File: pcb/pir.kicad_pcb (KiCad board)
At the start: 2 copper layers, 80 x 100 mm, 146 parts, among them IC1 MAX44009EDT+T, IC2 IRA-S210ST01, IC3 EL817S, IC4 EL817S, IC7 EL817S, IC8 EL817S, J1 SJ-2523-SMT-TR, J2 FH12-24S-0.5SH(55), J3 SWD, J4 UART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

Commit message: Routed what seem to be the last useful tracks
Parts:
- moved TP25 94.8 mm to (-145.8, 115.4)
- moved TP34 94.8 mm to (-141.7, 115.4)
- moved TP24 94.8 mm to (-137.2, 109.7)
- moved TP26 94.8 mm to (-133.1, 103.6)
- moved TP27 94.8 mm to (-146.9, 121.5)
- moved TP29 94.8 mm to (-151.0, 121.5)
- moved TP31 94.8 mm to (-155.1, 120.1)
- moved TP32 94.8 mm to (-137.2, 103.6)
- moved TP33 94.8 mm to (-159.1, 120.1)
- moved TP36 94.8 mm to (-129.0, 103.6)
- moved TP39 94.8 mm to (-133.6, 115.7)
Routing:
- net VCC: track 332.6 -> 444.3 mm, vias 4 -> 6
- net Net-(JP3-Pad2): track 15.6 -> 37.9 mm, vias 0 -> 1
- net Earth: track 18.7 -> 35.3 mm, vias 5 -> 6
- net /soc/EINK_MOSI: track 46.1 -> 49.3 mm
- net /sensor/OPAMP2+: track 38.6 -> 41.5 mm

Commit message: OK button MOVED TO A WKUP pin. PCB routing done.
DRC passed.
Unconnected tracks : 0.
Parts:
- removed TP24, TP25, TP26, TP27, TP31, TP32, TP33, TP34, TP36, TP39: TEST, Measurement_Points:Measurement_Point_Round-TH_Small
- TP11, TP12, TP13, TP15, TP16, TP17, TP18: footprint Measurement_Points:Measurement_Point_Round-TH_Small -> Measurement_Points:Measurement_Point_Round-SMD-Pad_Small
- moved TP29 267.1 mm to (108.4, 58.0)
- moved TP18 235.0 mm to (51.8, 66.4)
- moved TP17 232.3 mm to (53.6, 75.2)
- moved TP15 220.3 mm to (52.6, 71.6)
- moved TP12 218.2 mm to (50.2, 69.0)
- moved TP11 214.8 mm to (50.4, 74.6)
- moved TP13 206.0 mm to (48.0, 71.6)
- moved TP16 200.6 mm to (48.6, 65.6)
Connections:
- U1 pad 25: Net-(TP24-Pad1) -> /soc/OK
- U1 pad 39: /soc/OK -> Net-(U1-Pad39)
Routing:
- net /soc/OK: track 25.5 -> 33.0 mm
- net Earth: track 35.3 -> 41.7 mm, vias 6 -> 9
- net Net-(C41-Pad1): track 7.33 -> 11.7 mm
- net Net-(C8-Pad1): track 0.00 -> 3.62 mm
- net Net-(C38-Pad2): track 77.9 -> 81.1 mm
- net /soc/EINK_BS: track 46.0 -> 46.8 mm, vias 2 -> 3
- net /soc/EINK_D/C: track 39.9 -> 40.1 mm, vias 2 -> 3
- net VCC: track 444.3 -> 444.1 mm, vias 6 -> 7
- net /soc/EINK_SCK: vias 4 -> 5
- net /soc/EINK_MOSI: vias 2 -> 3
- net /soc/EINK_CS: vias 2 -> 3
- net /soc/EINK_BUSY: vias 2 -> 3
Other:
- rule trace_min: 0.1 -> 0.25

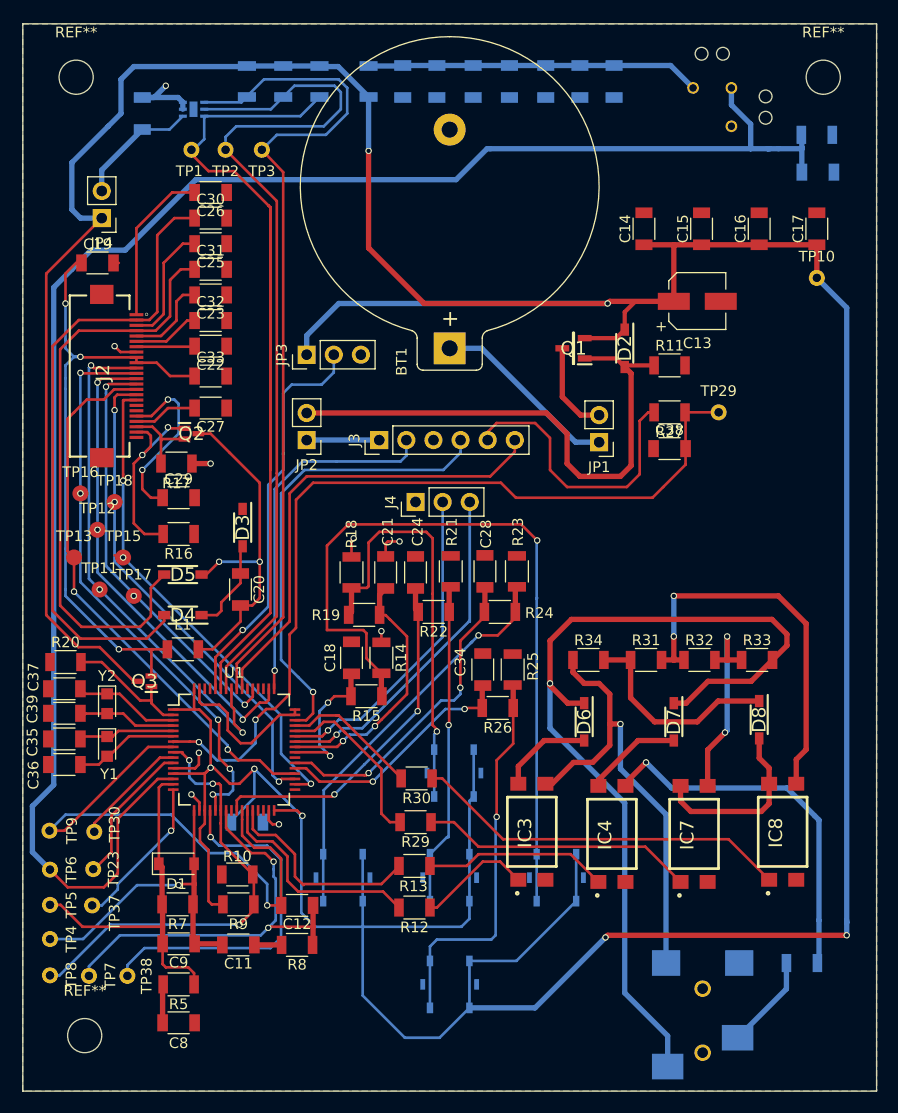
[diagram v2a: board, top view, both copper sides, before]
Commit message: 1 mounting hole was missing for some reason
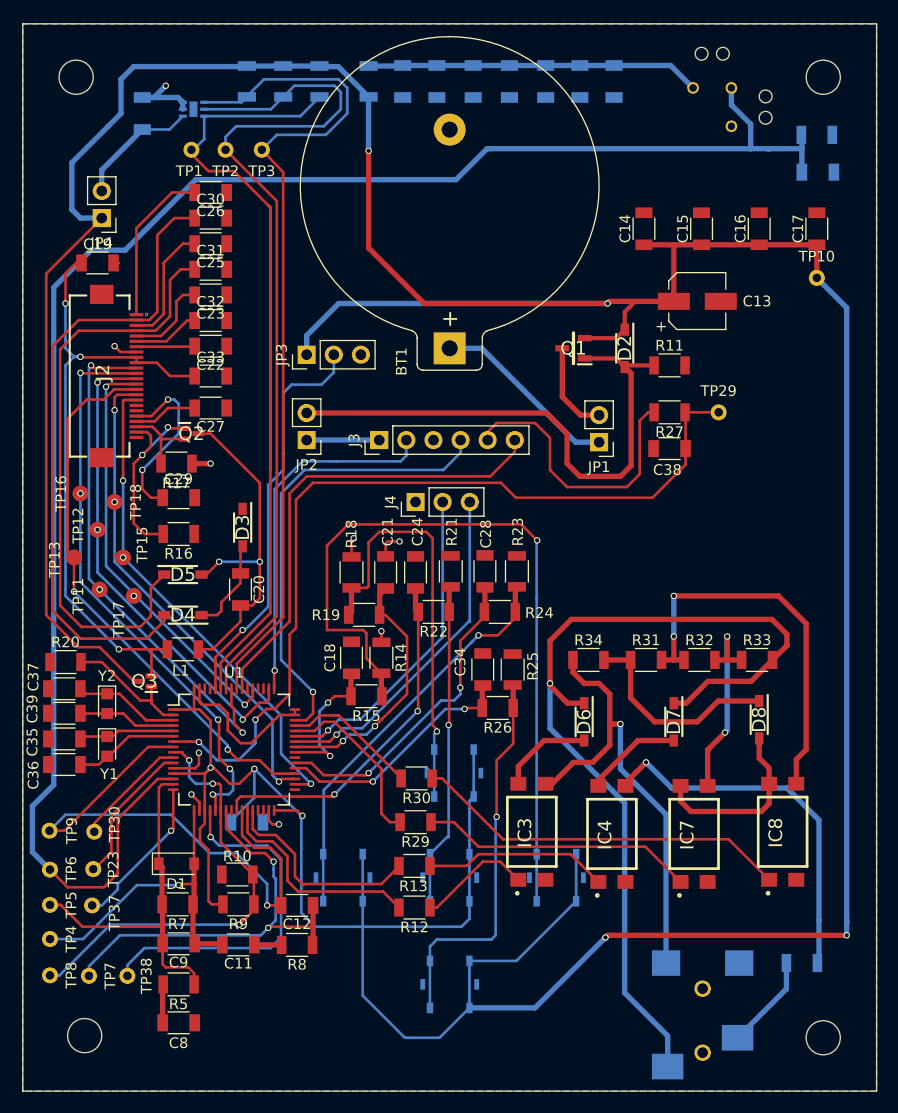
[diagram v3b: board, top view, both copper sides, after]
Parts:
- added REF**: MountingHole_3.2mm_M3, Mounting_Holes:MountingHole_3.2mm_M3, F.Cu at (118.2, 116.6)
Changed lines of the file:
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@@
     (tracks 1050)
     (zones 0)
-    (modules 136)
+    (modules 137)
     (nets 100)
   )
@@
     (add_net nRESET)
   )
+  (module Mounting_Holes:MountingHole_3.2mm_M3 locked (layer F.Cu)
+    (at 118.2 116.6)
+    (descr "Mounting Hole 3.2mm, no annular, M3")
+    (tags "mounting hole 3.2mm no annular m3")
+    (attr virtual)
+    (fp_text reference REF** (at 0 -4.2) (layer F.SilkS) hide
+      (effects (font (size 1 1) (thickness 0.15)))
+    )
+    (fp_text value MountingHole_3.2mm_M3 (at 0 4.2) (layer F.Fab)
+      (effects (font (size 1 1) (thickness 0.15)))
+    )
+    (fp_text user %R (at 0.3 0) (layer F.Fab)
+      (effects (font (size 1 1) (thickness 0.15)))
+    )
+    (fp_circle (center 0 0) (end 3.2 0) (layer Cmts.User) (width 0.15))
+    (fp_circle (center 0 0) (end 3.45 0) (layer F.CrtYd) (width 0.05))
+    (pad 1 np_thru_hole circle (at 0 0) (size 3.2 3.2) (drill 3.2) (layers *.Cu *.Mask))
+  )
   (module Capacitors_SMD:C_1206 (layer B.Cu)
     (at 64.2 96.4 180)
@@
     (tags "mounting hole 3.2mm no annular m3")
     (attr virtual)
-    (fp_text reference REF** (at 0 -4.2) (layer F.SilkS)
+    (fp_text reference REF** (at 0 -4.2) (layer F.SilkS) hide
       (effects (font (size 1 1) (thickness 0.15)))
     )
@@
     (tags "mounting hole 3.2mm no annular m3")
     (attr virtual)
-    (fp_text reference REF** (at 0 -4.2) (layer F.SilkS)
+    (fp_text reference REF** (at 0 -4.2) (layer F.SilkS) hide
       (effects (font (size 1 1) (thickness 0.15)))
     )
@@
     (descr "SMT capacitor, aluminium electrolytic, 5x5.3")
     (attr smd)
-    (fp_text reference C13 (at 0 3.92) (layer F.SilkS)
+    (fp_text reference C13 (at 5.6 0) (layer F.SilkS)
       (effects (font (size 1 1) (thickness 0.15)))
     )
@@
       (effects (font (size 1 1) (thickness 0.15)))
     )
-    (fp_text user %R (at 0 3.92) (layer F.Fab)
+    (fp_text user %R (at 0 0.2 90) (layer F.Fab)
       (effects (font (size 1 1) (thickness 0.15)))
     )
@@
     (tags "capacitor 1206")
     (attr smd)
-    (fp_text reference C38 (at 0 -1.75) (layer F.SilkS)
+    (fp_text reference C38 (at -0.2 2) (layer F.SilkS)
       (effects (font (size 1 1) (thickness 0.15)))
     )
@@
       (effects (font (size 1 1) (thickness 0.15)))
     )
-    (fp_text user %R (at 0 -1.75) (layer F.Fab)
+    (fp_text user %R (at 0 0) (layer F.Fab)
       (effects (font (size 1 1) (thickness 0.15)))
     )
@@
     (fp_line (start 1.8 4.35) (end 1.8 -1.8) (layer F.CrtYd) (width 0.05))
     (fp_line (start 1.8 -1.8) (end -1.8 -1.8) (layer F.CrtYd) (width 0.05))
-    (fp_text user %R (at 0 1.27 270) (layer F.Fab)
+    (fp_text user %R (at 0 1.2 270) (layer F.Fab)
       (effects (font (size 1 1) (thickness 0.15)))
     )
@@
     (tags "mounting hole 3.2mm no annular m3")
     (attr virtual)
-    (fp_text reference REF** (at 0 -4.2) (layer F.SilkS)
+    (fp_text reference REF** (at 0 -4.2) (layer F.SilkS) hide
       (effects (font (size 1 1) (thickness 0.15)))
     )
@@
     (tags "resistor 1206")
     (attr smd)
-    (fp_text reference L1 (at 0 -2.3) (layer F.SilkS)
+    (fp_text reference L1 (at -0.2 2) (layer F.SilkS)
       (effects (font (size 1 1) (thickness 0.15)))
     )
@@
     (tags "Mesurement Point Round SMD Pad 1.5mm")
     (attr virtual)
-    (fp_text reference TP11 (at 0 -2) (layer F.SilkS)
+    (fp_text reference TP11 (at -2 0.6 90) (layer F.SilkS)
       (effects (font (size 1 1) (thickness 0.15)))
     )
@@
     (tags "Mesurement Point Round SMD Pad 1.5mm")
     (attr virtual)
-    (fp_text reference TP12 (at 0 -2) (layer F.SilkS)
+    (fp_text reference TP12 (at -1.8 -0.4 90) (layer F.SilkS)
       (effects (font (size 1 1) (thickness 0.15)))
     )
@@
     (tags "Mesurement Point Round SMD Pad 1.5mm")
     (attr virtual)
-    (fp_text reference TP13 (at 0 -2) (layer F.SilkS)
+    (fp_text reference TP13 (at -1.8 0.2 90) (layer F.SilkS)
       (effects (font (size 1 1) (thickness 0.15)))
     )
@@
     (tags "Mesurement Point Round SMD Pad 1.5mm")
     (attr virtual)
-    (fp_text reference TP15 (at 0 -2) (layer F.SilkS)
+    (fp_text reference TP15 (at 1.8 -1.2 90) (layer F.SilkS)
       (effects (font (size 1 1) (thickness 0.15)))
     )
@@
     (tags "Mesurement Point Round SMD Pad 1.5mm")
     (attr virtual)
-    (fp_text reference TP16 (at 0 -2) (layer F.SilkS)
+    (fp_text reference TP16 (at -1.8 0 90) (layer F.SilkS)
       (effects (font (size 1 1) (thickness 0.15)))
     )
@@
     (tags "Mesurement Point Round SMD Pad 1.5mm")
     (attr virtual)
-    (fp_text reference TP17 (at 0 -2) (layer F.SilkS)
+    (fp_text reference TP17 (at -1.4 2.2 90) (layer F.SilkS)
       (effects (font (size 1 1) (thickness 0.15)))
     )
@@
     (tags "Mesurement Point Round SMD Pad 1.5mm")
     (attr virtual)
-    (fp_text reference TP18 (at 0 -2) (layer F.SilkS)
+    (fp_text reference TP18 (at 2 0 90) (layer F.SilkS)
       (effects (font (size 1 1) (thickness 0.15)))
     )

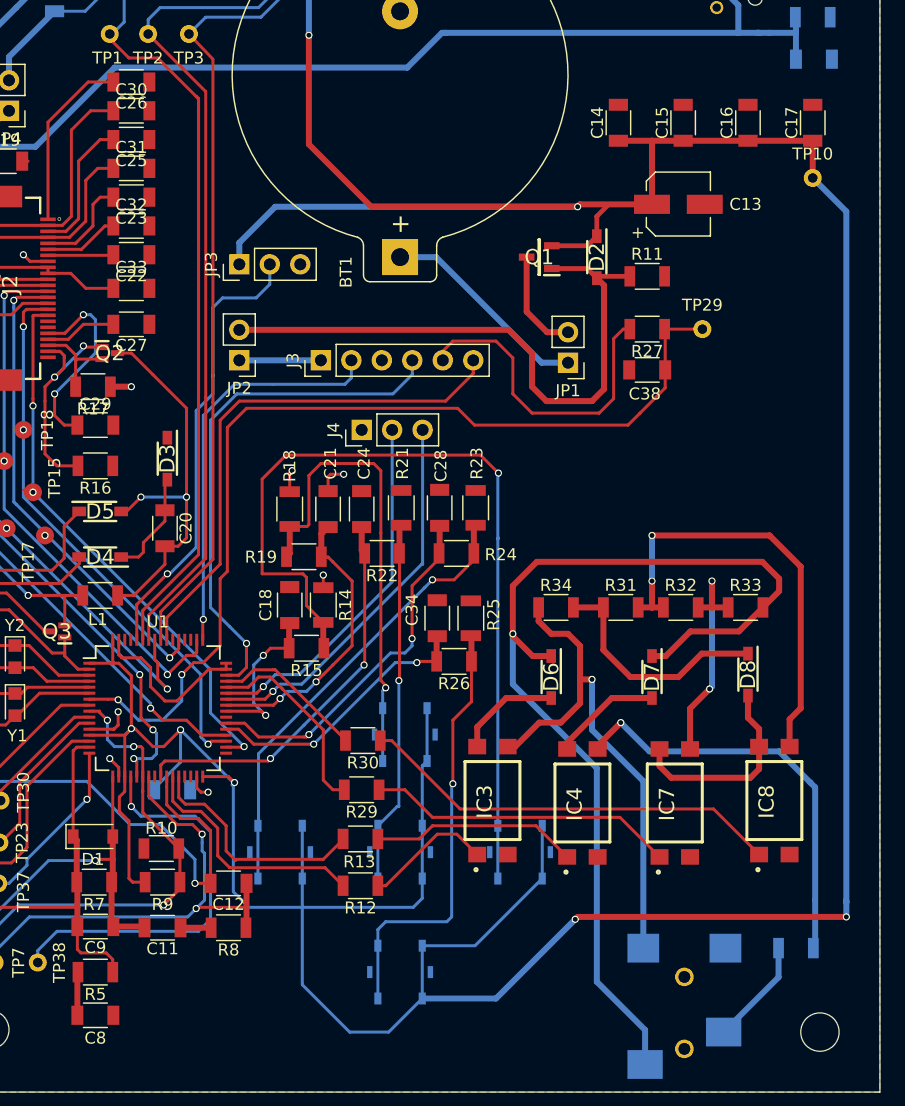
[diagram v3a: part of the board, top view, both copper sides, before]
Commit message: Changed buttons from Panasonic to C&K
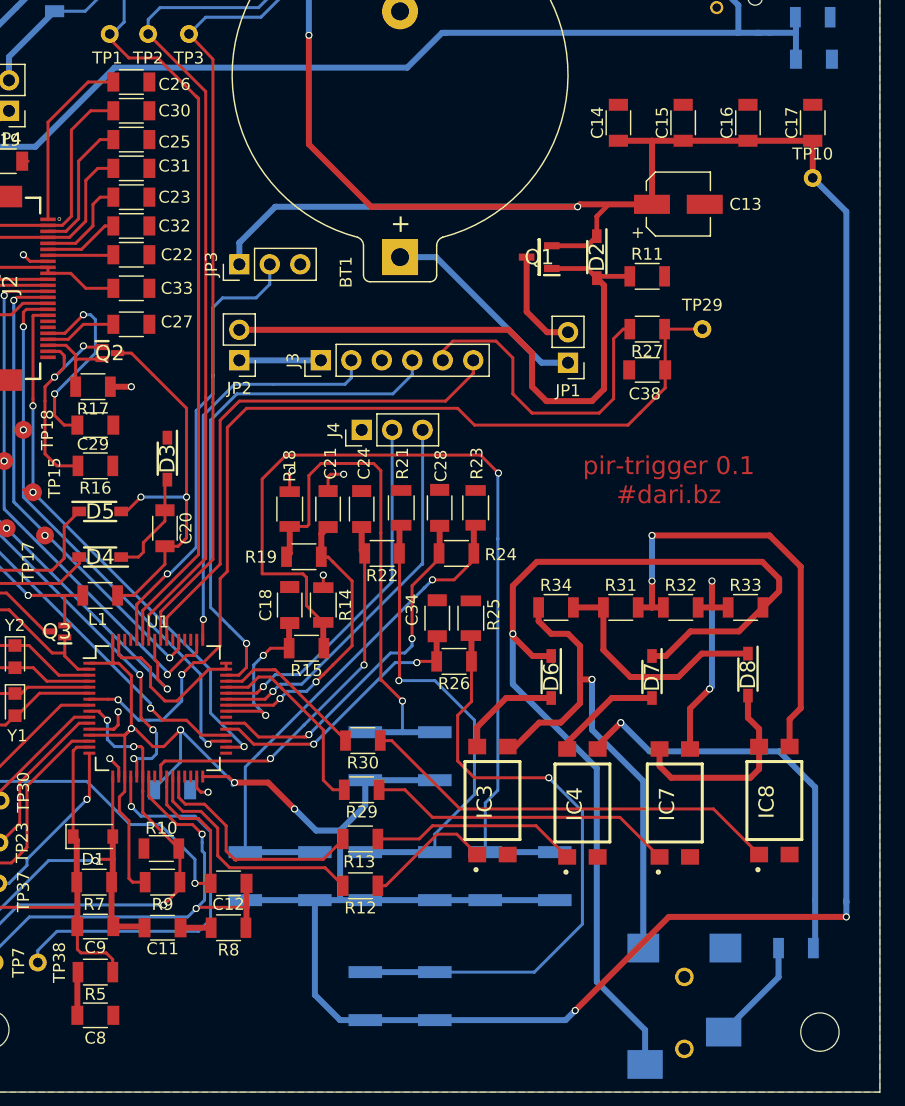
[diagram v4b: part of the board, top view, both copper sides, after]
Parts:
- SW1, SW2, SW3, SW4, SW5: value SW_Push -> SW_DPST-KSC931; footprint Buttons_Switches_SMD:SW_SPST_Panasonic_EVQPL_3PL_5PL_PT_A08 -> KSC931J_LFS:KSC8(J)
- moved SW1 2.00 mm to (93.2, 103.6)
- moved SW3 2.00 mm to (83.2, 103.6)
- moved SW4 2.00 mm to (73.2, 103.6)
- moved SW5 2.00 mm to (83.2, 113.6)
- moved SW2 1.84 mm to (83.2, 93.6)
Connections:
- SW1 pad 1: Net-(R14-Pad2) -> VCC
- SW1 pad 2: VCC -> Net-(R14-Pad2)
- SW2 pad 1: Net-(R18-Pad2) -> VCC
- SW2 pad 2: VCC -> Net-(R18-Pad2)
- SW3 pad 1: Net-(R21-Pad2) -> VCC
- SW3 pad 2: VCC -> Net-(R21-Pad2)
- SW4 pad 1: Net-(R23-Pad2) -> VCC
- SW4 pad 2: VCC -> Net-(R23-Pad2)
- SW5 pad 1: Net-(R25-Pad2) -> VCC
- SW5 pad 2: VCC -> Net-(R25-Pad2)
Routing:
- net VCC: track 444.1 -> 426.8 mm, vias 7 -> 8
- net Net-(R25-Pad2): track 36.5 -> 52.2 mm
- net Net-(R21-Pad2): track 30.3 -> 38.9 mm
- net Net-(R23-Pad2): track 38.2 -> 42.3 mm
- net Net-(R18-Pad2): track 39.5 -> 43.5 mm
- net Net-(R14-Pad2): track 73.3 -> 77.3 mm
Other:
- board text added: "pir-trigger 0.1 #dari.bz"
